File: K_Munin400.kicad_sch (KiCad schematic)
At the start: 60 parts, among them IC1 LMC660AIM_NOPB, IC2 ACHS-7123-000E, J1 Conn_Coaxial, J2 Conn_Coaxial, J3 Conn_02x03_Odd_Even, Q1 MRF300AN, Q3 MRF300BN, Q4 BSS84, T1 Transformer_1P_1S, T2 Transformer_1P_1S, T3 Transformer_1P_1S, T4 Transformer_1P_1S, U1 LM358, U2 LM78M05_TO252

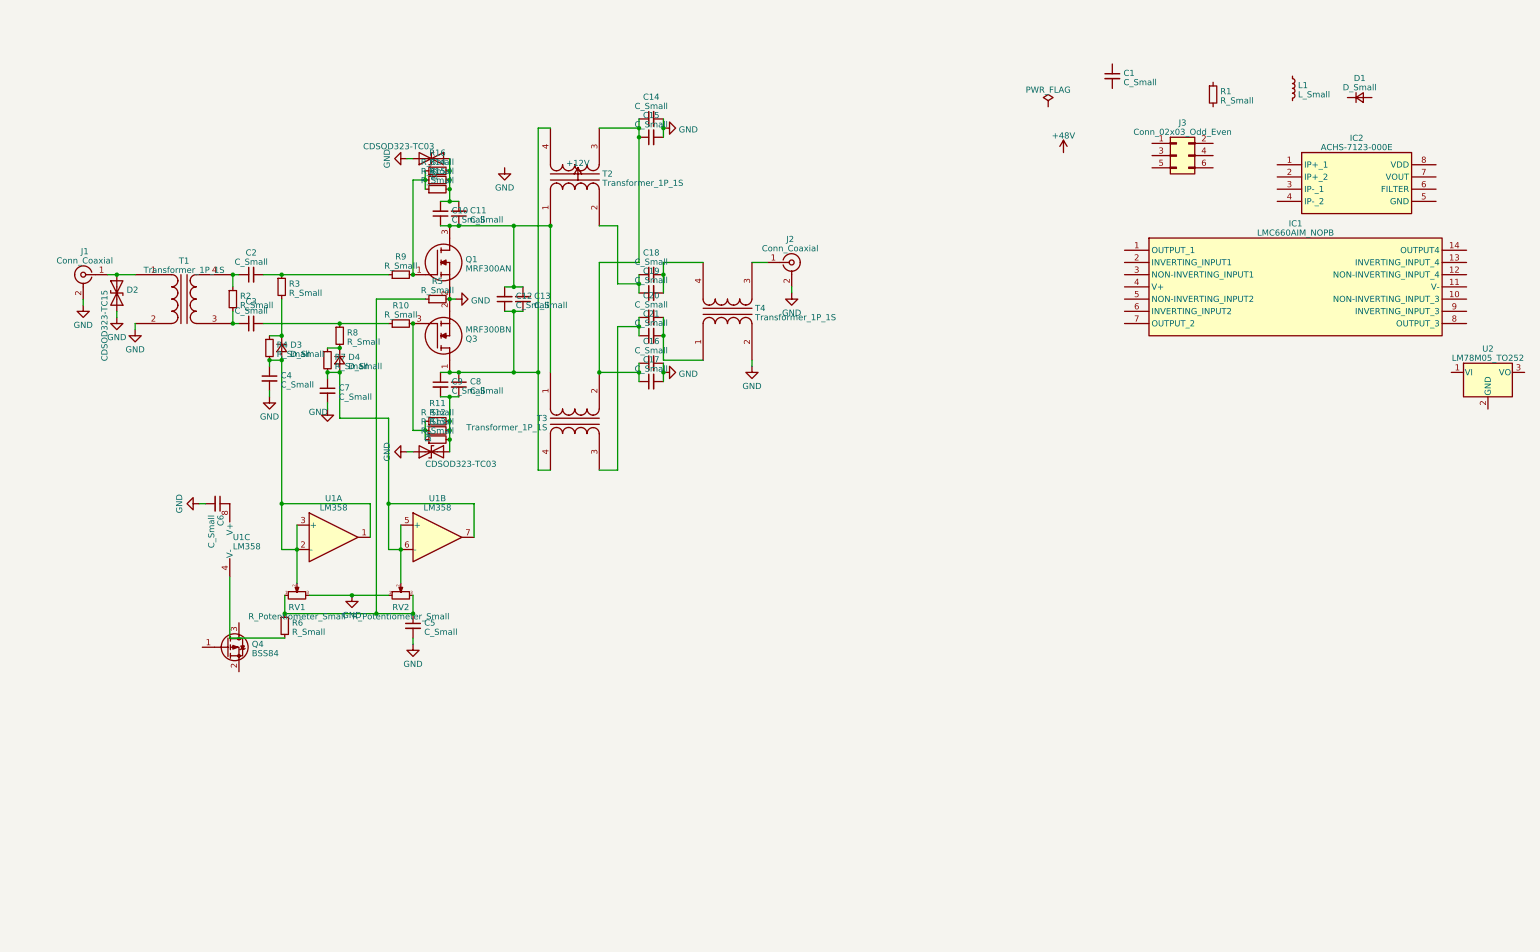
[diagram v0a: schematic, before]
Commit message: schematic completed, footprints not yet defined
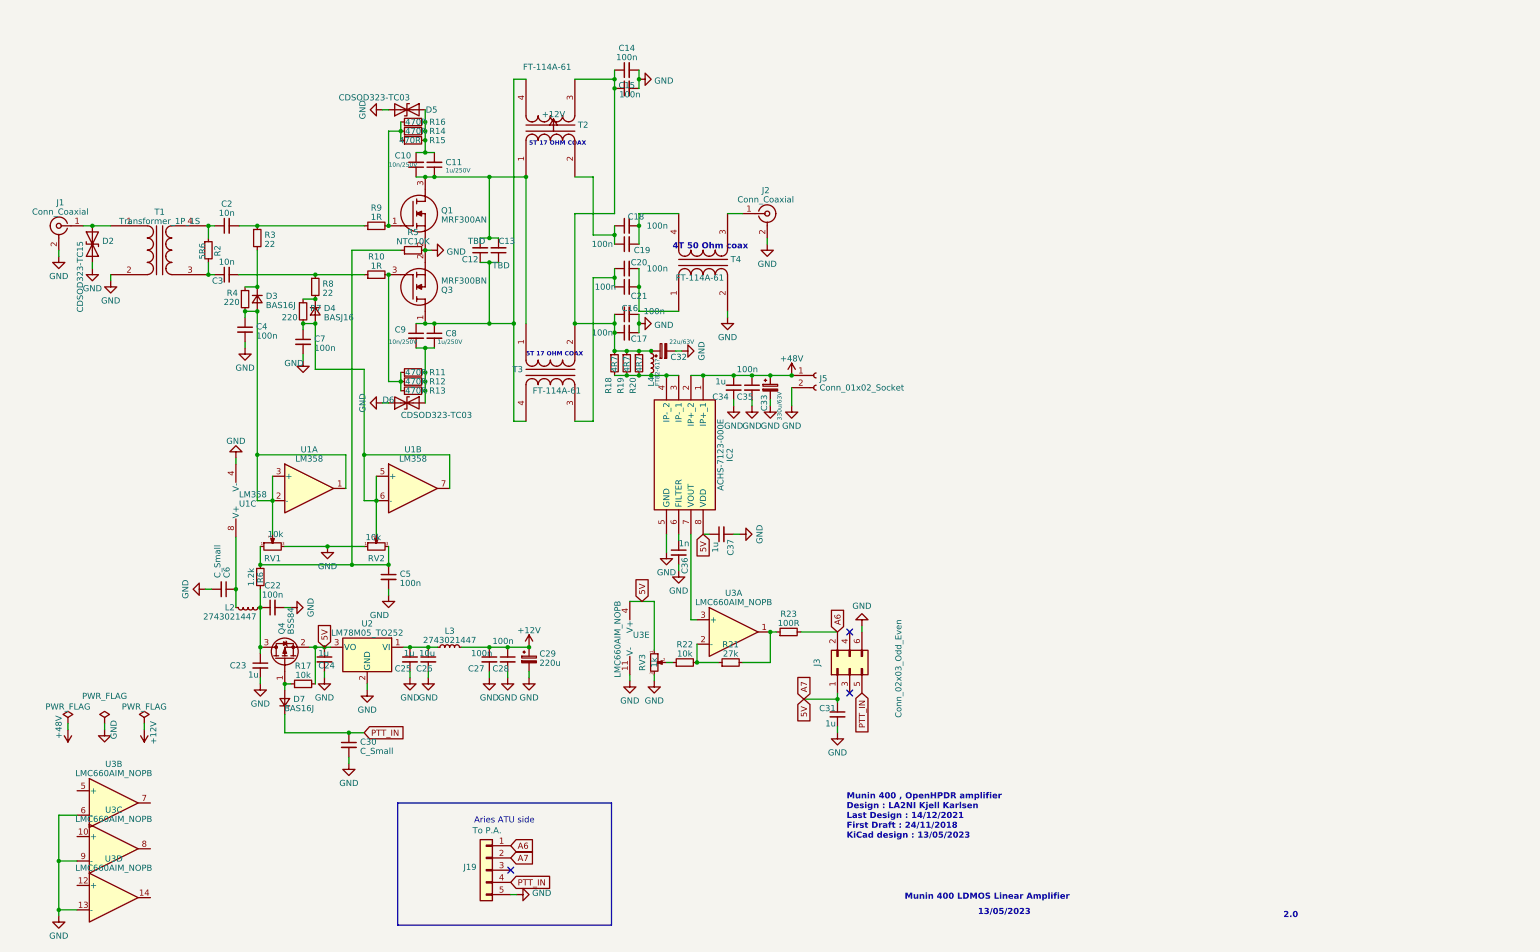
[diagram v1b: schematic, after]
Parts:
- removed C1: C_Small, symbol Device:C_Small
- removed D1: D_Small, symbol Device:D_Small
- removed IC1: LMC660AIM_NOPB, SOIC127P600X175-14N, symbol LMC660AIM_NOPB:LMC660AIM_NOPB
- removed L1: L_Small, symbol Device:L_Small
- removed R1: R_Small, symbol Device:R_Small
- added C22, C27, C28, C35: 100n, symbol Device:C_Small
- added C23, C24, C25, C31, C34, C37: 1u, symbol Device:C_Small
- added C26: 10u, symbol Device:C_Small
- added C29: 220u, symbol Device:C_Polarized_Small
- added C30: C_Small, symbol Device:C_Small
- added C32: 22u/63V, symbol Device:C_Polarized_Small
- added C33: 330u/63V, symbol Device:C_Polarized_Small
- added C36: 1n, symbol Device:C_Small
- added D7: BAS16J, symbol Device:D_Small
- added J19: To P.A., Connector_Molex:Molex_KK-254_AE-6410-05A_1x05_P2.54mm_Vertical, symbol Connector_Generic:Conn_01x05
- added J5: Conn_01x02_Socket, symbol Connector:Conn_01x02_Socket
- added L2, L3: 2743021447, symbol Device:L_Small
- added L4: FT82-61?, symbol Device:L_Small
- added R17, R22: 10k, symbol Device:R_Small
- added R18, R19, R20: 4R7, symbol Device:R_Small
- added R21: 27k, symbol Device:R_Small
- added R23: 100R, symbol Device:R_Small
- added RV3: 1k, symbol Device:R_Potentiometer_Small
- added U3: LMC660AIM_NOPB, Package_SO:SOIC-14_3.9x8.7mm_P1.27mm, symbol Amplifier_Operational:TL074
- C10, C9: value C_Small -> 10n/250V
- C11, C8: value C_Small -> 1u/250V
- C12, C13: value C_Small -> TBD
- C14, C15, C16, C17, C18, C19, C20, C21, C4, C5, C7: value C_Small -> 100n
- C2, C3: value C_Small -> 10n
- D3: value D_Small -> BAS16J
- D4: value D_Small -> BASJ16
- IC2: footprint SOIC127P606X204-8N -> Package_SO:SOIC-8_7.5x5.85mm_P1.27mm
- R10, R9: value R_Small -> 1R
- R11, R12, R13, R14, R15, R16: value R_Small -> 470R
- R2: value R_Small -> 5R6
- R3, R8: value R_Small -> 22
- R4, R7: value R_Small -> 220
- R5: value R_Small -> NTC10K
- R6: value R_Small -> 1.2k
- RV1, RV2: value R_Potentiometer_Small -> 10k
- T2, T3, T4: value Transformer_1P_1S -> FT-114A-61
- U1: footprint (none) -> Package_SO:SOIC-8_7.5x5.85mm_P1.27mm
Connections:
- net +12V: now also C27.1, C28.1, C29.1, L3.1
- net +48V: now also IC2.1 (IP+_1), IC2.2 (IP+_2), C33.1, C34.1, C35.1, J5.1 (Pin_1)
- net GND: now also IC2.5 (GND), J3.6 (Pin_6), U1.4 (V-), U2.2 (GND), C22.2, C23.2, C24.2, C25.2, C26.2, C27.2, C28.2, C29.2, C30.2, C31.2, C32.2, C33.2, C34.2, C35.2, C36.2, C37.2, J19.5 (Pin_5), J5.2 (Pin_2), RV3.3, U3.11 (V-), U3.13 (-), U3.6 (-), U3.9 (-)
- net at C14.1, C15.1, C16.1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: now also C32.1, L4.2, R18.1, R19.1, R20.1
- net at C6.1, U1.8 (V+): now also L2.1
- net at Q4.1 (G): now also D7.2 (A), R17.1
- net 5V: now reaches Q4.2 (S)
- net 5V: now also IC2.8 (VDD), J3.1 (Pin_1), U2.3 (VO), C24.1, C31.1, C37.1, J19.2 (Pin_2), R17.2, RV3.1, U3.4 (V+)
- net at Q4.3 (D): now also R6.2, C22.1, C23.1, L2.2
- net A6: now reaches J3.2 (Pin_2)
- net A6: now also J19.1 (Pin_1), R23.2
- net PTT_IN: now reaches J3.5 (Pin_5)
- net PTT_IN: now also C30.1, D7.1 (K), J19.4 (Pin_4)
- net at U2.1 (VI): now also C25.1, C26.1, L3.2
- net at IC2.3 (IP-_1): now also IC2.4 (IP-_2), L4.1, R18.2, R19.2, R20.2
- net at IC2.6 (FILTER): now also C36.1
- net at IC2.7 (VOUT): now also U3.3 (+)
- new net: R21.2, R23.1, U3.1
- new net: R21.1, R22.2, U3.2 (-)
- new net: R22.1, RV3.2
- no-connect marks 0 -> 3
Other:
- note added: "13/05/2023"
- note added: "2.0"
- note added: "4T 50 Ohm coax"
- note added: "5T 17 OHM COAX"
- note added: "Aries ATU side"
- note added: "Munin 400 , OpenHPDR amplifier Design : LA2NI Kjell Karlsen Last Design : 14/12/2021 First Draft : 24/11/2018 KiCad design : 13/05/2023"
- note added: "Munin 400 LDMOS Linear Amplifier"
- moved on the sheet: C10, C11, C12, C13, C14, C15, C16, C17, C18, C19, C2, C20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

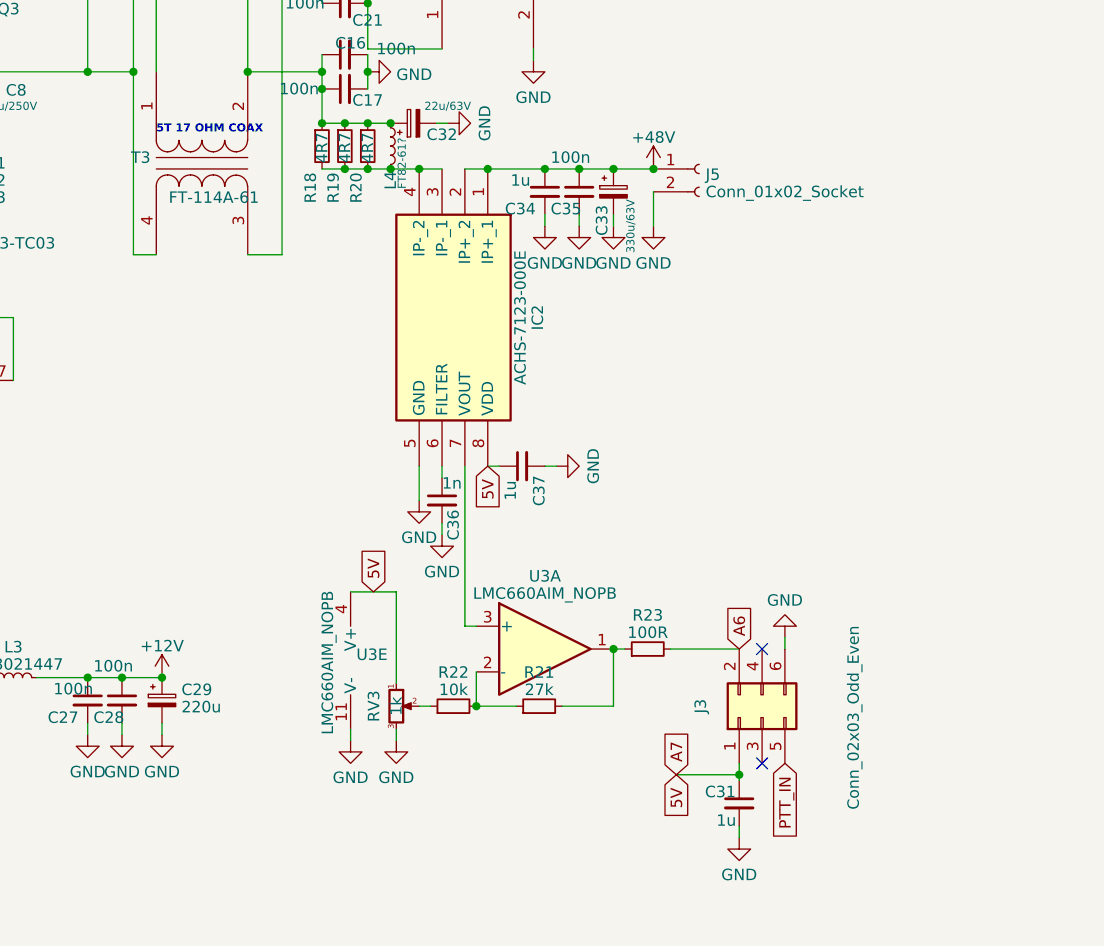
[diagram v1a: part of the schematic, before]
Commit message: schematic completed, footprint not yet configured
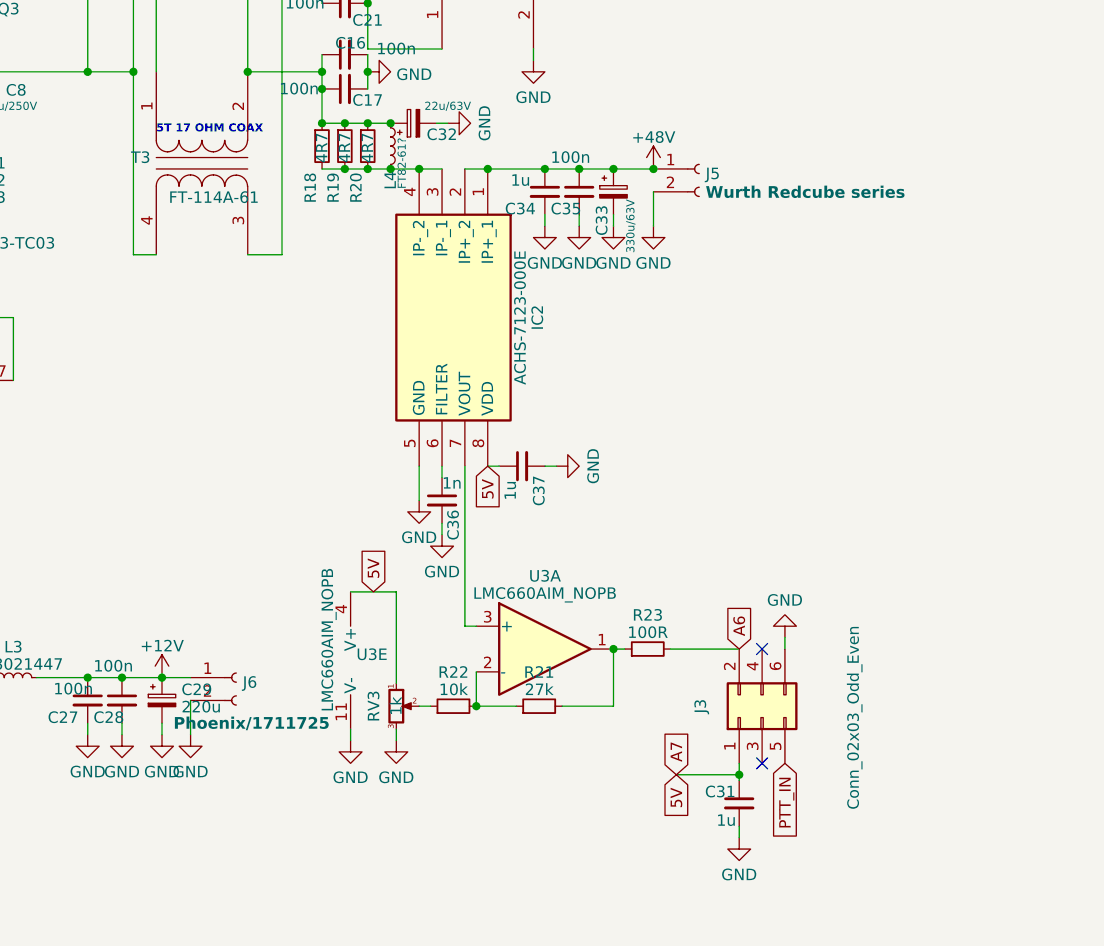
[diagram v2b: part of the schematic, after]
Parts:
- added J6: Phoenix/1711725, symbol Connector:Conn_01x02_Socket
- J5: value Conn_01x02_Socket -> Wurth Redcube series
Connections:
- net +12V: now also J6.1 (Pin_1)
- net GND: now also J6.2 (Pin_2)
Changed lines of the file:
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@@
     (stroke (width 0) (type default))
   )
+  (wire (pts (xy 116.205 140.335) (xy 116.205 144.145))
+    (stroke (width 0) (type default))
+  )
   (wire (pts (xy 53.975 67.945) (xy 56.515 67.945))
     (stroke (width 0) (type default))
@@
     (stroke (width 0) (type default))
   )
+  (wire (pts (xy 113.03 137.795) (xy 116.205 137.795))
+    (stroke (width 0) (type default))
+  )
   (wire (pts (xy 152.4 140.97) (xy 147.955 140.97))
     (stroke (width 0) (type default))
@@
     )
   )
+  (symbol (lib_id "Connector:Conn_01x02_Socket") (at 121.285 137.795 0) (unit 1)
+    (in_bom yes) (on_board yes) (dnp no)
+    (property "Reference" "J6" (at 121.9962 138.3335 0)
+      (effects (font (size 1.27 1.27)) (justify left))
+    )
+    (property "Value" "Phoenix/1711725" (at 114.3 142.875 0)
+      (effects (font (size 1.3 1.3) bold (color 255 21 0 1)) (justify left))
+    )
+    (property "Footprint" "" (at 121.285 137.795 0)
+      (effects (font (size 1.27 1.27)) hide)
+    )
+    (property "Datasheet" "~" (at 121.285 137.795 0)
+      (effects (font (size 1.27 1.27)) hide)
+    )
+    (pin "1")
+    (pin "2")
+    (instances
+      (project "K_Munin400"
+        (path "/8660a1ca-0bbf-4bd1-bcf7-983d207c8f33"
+          (reference "J6") (unit 1)
+        )
+      )
+    )
+  )
   (symbol (lib_id "Amplifier_Operational:TL074") (at 26.67 179.705 0) (unit 3)
     (in_bom yes) (on_board yes) (dnp no) (fields_autoplaced)
@@
       (effects (font (size 1.27 1.27)) (justify left))
     )
-    (property "Value" "LMC660AIM_NOPB" (at 131.445 144.145 90)
+    (property "Value" "LMC660AIM_NOPB" (at 131.445 141.605 90)
       (effects (font (size 1.27 1.27)) (justify left))
     )
@@
   (symbol (lib_id "Connector:Conn_01x02_Socket") (at 172.72 81.28 0) (unit 1)
     (in_bom yes) (on_board yes) (dnp no) (fields_autoplaced)
-    (property "Reference" "J5" (at 173.4312 81.9063 0)
+    (property "Reference" "J5" (at 173.4312 81.8185 0)
       (effects (font (size 1.27 1.27)) (justify left))
     )
-    (property "Value" "Conn_01x02_Socket" (at 173.4312 83.8273 0)
-      (effects (font (size 1.27 1.27)) (justify left))
+    (property "Value" "Wurth Redcube series" (at 173.4312 83.881 0)
+      (effects (font (size 1.3 1.3) bold (color 255 21 0 1)) (justify left))
     )
     (property "Footprint" "" (at 172.72 81.28 0)
@@
         )
       )
+    )
+  )
+  (symbol (lib_id "power:GND") (at 116.205 144.145 0) (unit 1)
+    (in_bom yes) (on_board yes) (dnp no) (fields_autoplaced)
+    (property "Reference" "#PWR03" (at 116.205 150.495 0)
+      (effects (font (size 1.27 1.27)) hide)
+    )
+    (property "Value" "GND" (at 116.205 148.2805 0)
+      (effects (font (size 1.27 1.27)))
+    )
+    (property "Footprint" "" (at 116.205 144.145 0)
+      (effects (font (size 1.27 1.27)) hide)
+    )
+    (property "Datasheet" "" (at 116.205 144.145 0)
+      (effects (font (size 1.27 1.27)) hide)
+    )
+    (pin "1")
+    (instances
+      (project "K_Munin400"
+        (path "/8660a1ca-0bbf-4bd1-bcf7-983d207c8f33"
+          (reference "#PWR03") (unit 1)
+        )
+      )
